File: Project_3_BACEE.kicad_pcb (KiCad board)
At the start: 2 copper layers, 42.2 x 27.4 mm, 17 parts, among them J1 Digital pins, J2 Serial, J3 ICSP, J4 I2C, U1 24LC1025, U2 24LC1025, U3 DS1337S+, U4 ATMEGA328P-AU, Y1 Crystal 32 MHz, Y2 Crystal 16 MHz

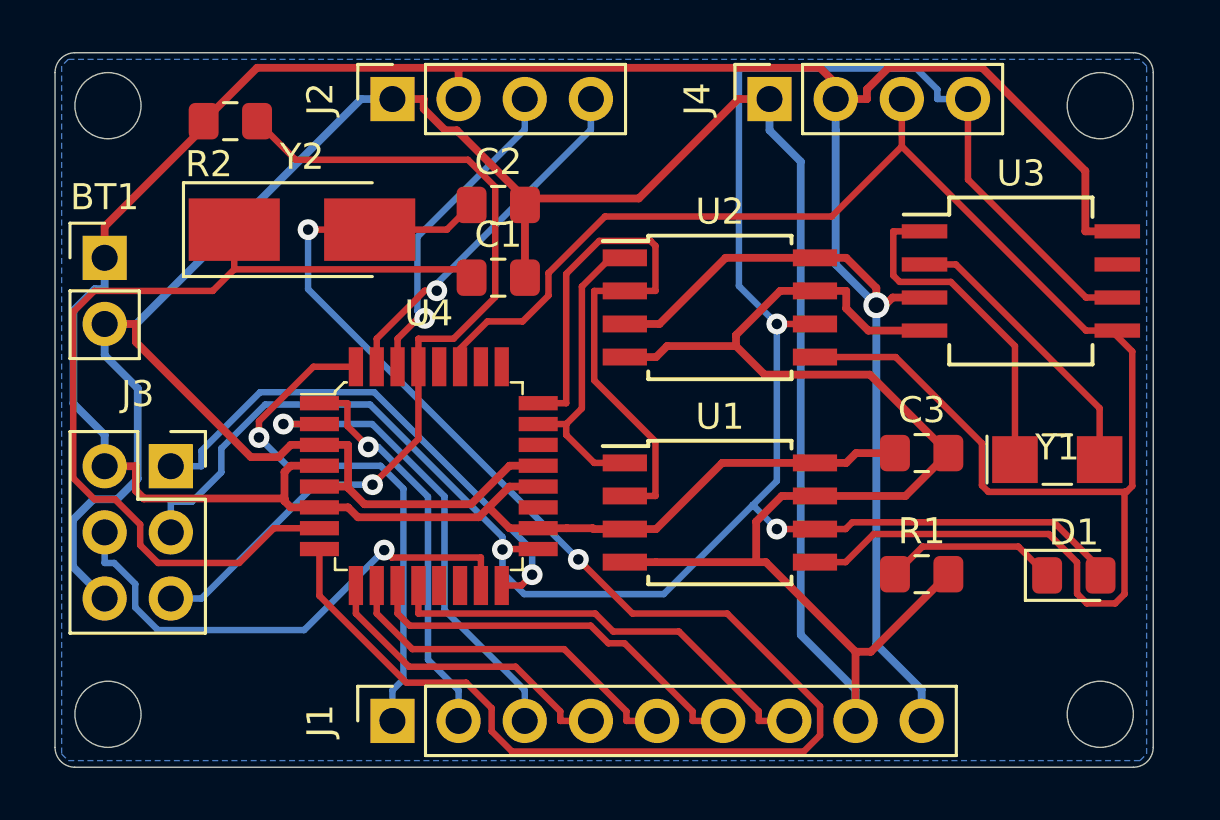
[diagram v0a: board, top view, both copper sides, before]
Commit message: Completed work in silkscreen.
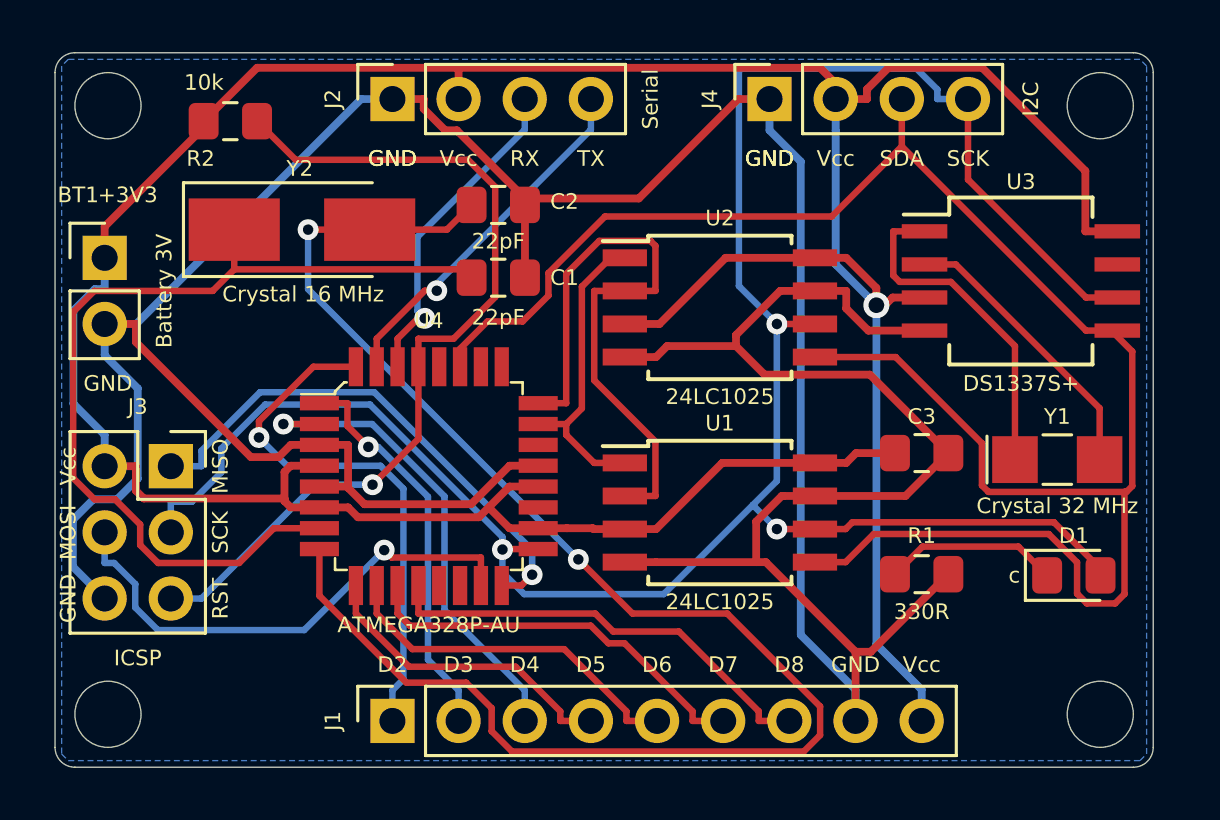
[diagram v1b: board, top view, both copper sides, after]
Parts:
- added G***: LOGO, FTS_Logo:FTS_Logo_18.9x7.4mm, B.Cu at (125.2, 93.5)
- added REF**: WEEE-Logo_4.2x6mm_SilkScreen, Symbol:WEEE-Logo_4.2x6mm_SilkScreen, B.Cu at (146.1, 93.0)
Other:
- board text added: "+3V3"
- board text added: "BACEE - 2Mbit EEPROM - Clock & callendar - UART, I2C, SPI, GPIO"
- board text added: "D2"
- board text added: "D3"
- board text added: "D4"
- board text added: "D5"
- board text added: "D6"
- board text added: "D7"
- board text added: "D8"
- board text added: "GND"
- board text added: "MISO"
- board text added: "MOSI"
- board text added: "RST"
- board text added: "RX"
- board text added: "SCK"
- board text added: "SDA"
- board text added: "TX"
- board text added: "Vcc"
- board text added: "c"

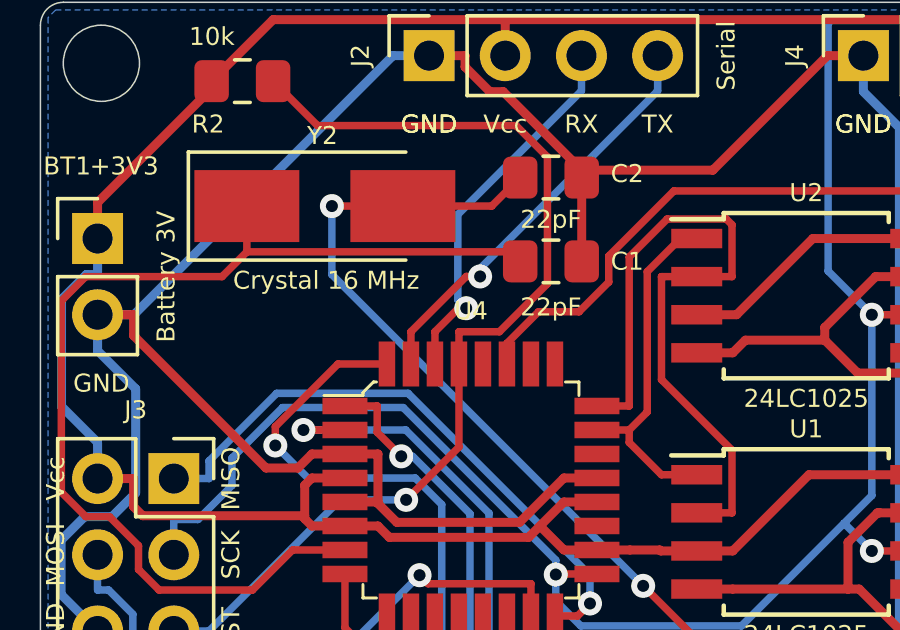
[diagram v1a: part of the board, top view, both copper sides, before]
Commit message: Added fully silkscreen and logos.
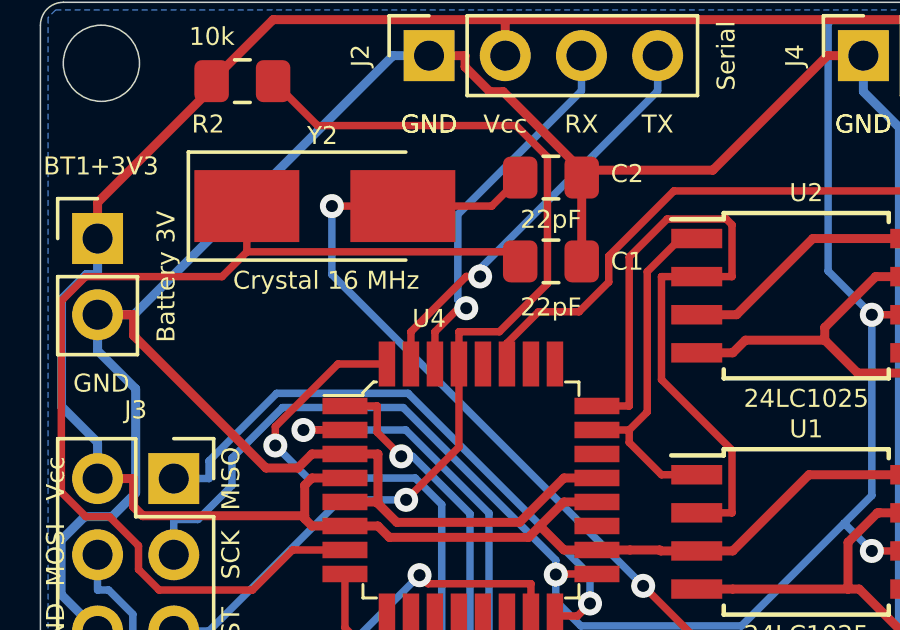
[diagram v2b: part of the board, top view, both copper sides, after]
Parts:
- moved REF** 29.5 mm to (119.9, 106.7), turned to 180 degrees
- moved G*** 19.8 mm to (140.8, 105.7), turned to 180 degrees
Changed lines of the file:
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@@
   )
   (module Symbol:WEEE-Logo_4.2x6mm_SilkScreen (layer B.Cu)
-    (at 146.05 92.964)
+    (at 119.888 106.68 180)
     (descr "Waste Electrical and Electronic Equipment Directive")
     (tags "Logo WEEE")
@@
   )
   (module FTS_Logo:FTS_Logo_18.9x7.4mm (layer B.Cu)
-    (at 125.222 93.472)
+    (at 140.843 105.664 180)
     (fp_text reference G*** (at 0 0) (layer B.SilkS) hide
       (effects (font (size 1.524 1.524) (thickness 0.3)) (justify mirror))
@@
     (descr http://www.atmel.com/Images/Atmel-8826-SEEPROM-PCB-Mounting-Guidelines-Surface-Mount-Packages-ApplicationNote.pdf)
     (attr smd)
-    (fp_text reference U4 (at 0 -5.969) (layer F.SilkS)
+    (fp_text reference U4 (at -1.397 -5.715) (layer F.SilkS)
       (effects (font (size 0.6 0.6) (thickness 0.15)))
     )
@@
     )
   )
-  (gr_text "BACEE\n- 2Mbit EEPROM\n- Clock & callendar\n- UART, I2C, SPI, GPIO" (at 118.11 105.918 180) (layer B.SilkS)
+  (gr_text "BACEE\n- 2Mbit EEPROM\n- Clock & callendar\n- UART, I2C, SPI, GPIO" (at 149.86 92.075) (layer B.SilkS)
     (effects (font (size 0.6 0.6) (thickness 0.15)) (justify left mirror))
   )

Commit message: Added gerber files for manufacturing.
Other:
- board text added: "BACEE - 2Mbit EEPROM - Clock & calendar - UART, I2C, SPI, GPIO"
- board text removed: "BACEE - 2Mbit EEPROM - Clock & callendar - UART, I2C, SPI, GPIO"
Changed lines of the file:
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@@
     (pcbplotparams
       (layerselection 0x010fc_ffffffff)
-      (usegerberextensions false)
+      (usegerberextensions true)
       (usegerberattributes false)
       (usegerberadvancedattributes false)
@@
       (outputformat 1)
       (mirror false)
-      (drillshape 1)
+      (drillshape 0)
       (scaleselection 1)
-      (outputdirectory ""))
+      (outputdirectory "BACEE_Gerber/"))
   )
   (net 0 "")
@@
     )
   )
-  (gr_text "BACEE\n- 2Mbit EEPROM\n- Clock & callendar\n- UART, I2C, SPI, GPIO" (at 149.86 92.075) (layer B.SilkS)
+  (gr_text "BACEE\n- 2Mbit EEPROM\n- Clock & calendar\n- UART, I2C, SPI, GPIO" (at 149.86 92.075) (layer B.SilkS)
     (effects (font (size 0.6 0.6) (thickness 0.15)) (justify left mirror))
   )
